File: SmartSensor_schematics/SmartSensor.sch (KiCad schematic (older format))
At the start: 47 parts, among them IC1 DS1337+, J1 Conn_01x07_Female, J3 Conn_02x04_Odd_Even, J4 FTDI cable connector, J6 Barrel_Jack, J8 6 PIN ISP, Q1 MMBF170, Q2 MMBF170, Q3 MMBF170, Q4 MMBF170, Q5 MMBF170, SW1 SW_Push, U1 AZ1117-3.3, U2 MCP9808_MSOP, U3 DMG2301l, U4 ATmega328-PU, U5 XBee_SMT, U6 MCP1640BCH, X1 XTAL

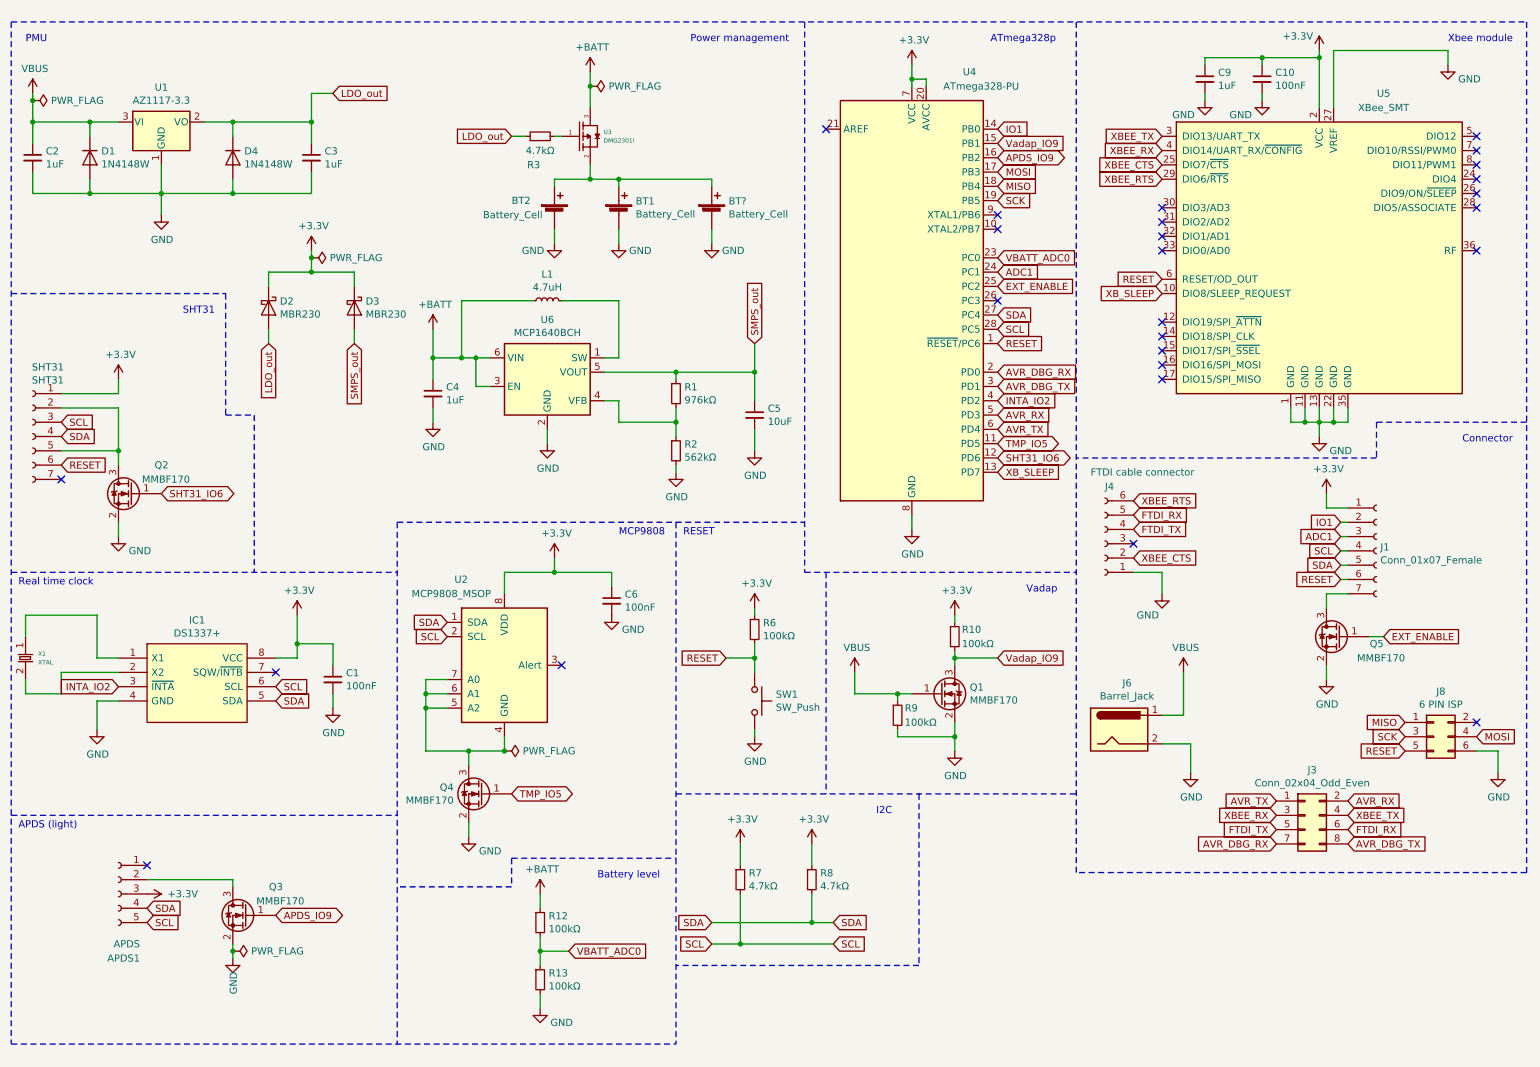
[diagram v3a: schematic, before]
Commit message: schematics: implement smart sensor v4
Implement version 4 in hardware.

Signed-off-by: Michel Megens <michel@michelmegens.net>
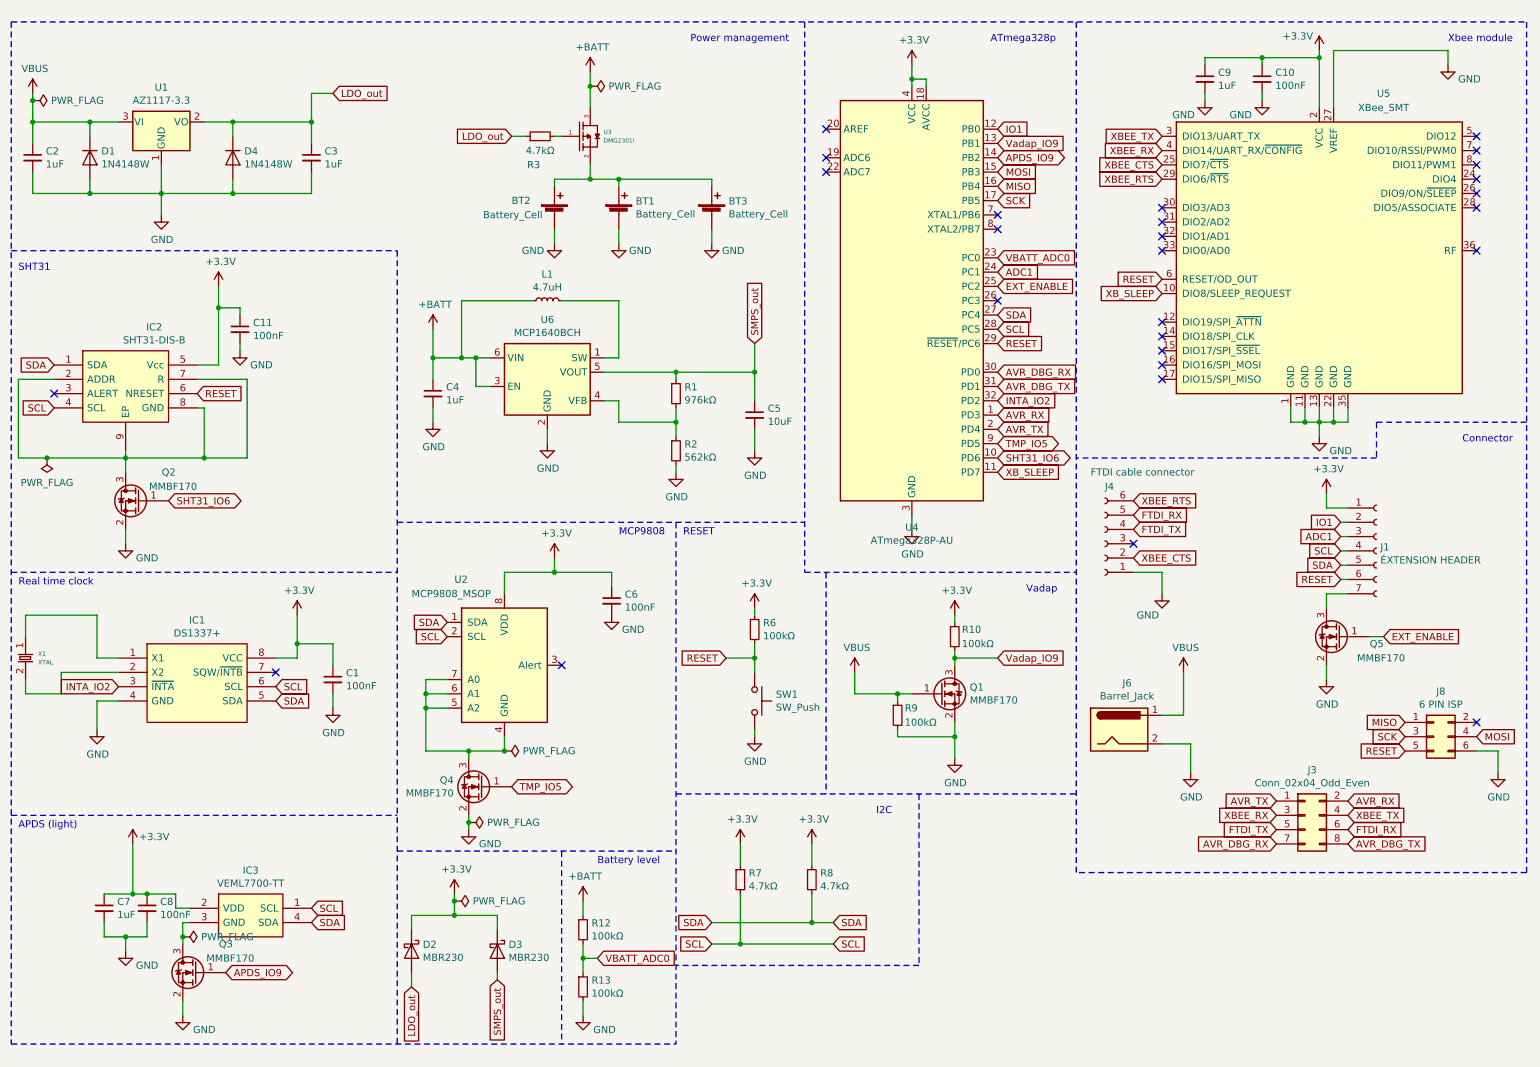
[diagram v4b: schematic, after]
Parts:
- removed APDS1: APDS, Connector_PinHeader_2.54mm:PinHeader_1x05_P2.54mm_Vertical, symbol Connector:Conn_01x05_Female
- removed SHT31: SHT31, Connector_PinHeader_2.54mm:PinHeader_1x07_P2.54mm_Vertical, symbol Connector:Conn_01x07_Female
- removed U4: ATmega328-PU, Package_DIP:DIP-28_W7.62mm, symbol MCU_Microchip_ATmega:ATmega328-PU
- added C11, C8: 100nF, Capacitor_SMD:C_1206_3216Metric_Pad1.42x1.75mm_HandSolder, symbol Device:C_Small
- added C7: 1uF, Capacitor_SMD:C_1206_3216Metric_Pad1.42x1.75mm_HandSolder, symbol Device:C_Small
- added IC2: SHT31-DIS-B, SHT31-DIS-B:SON50P250X250X90-9N-D, symbol SHT31-DIS-B:SHT31-DIS-B
- added IC3: VEML7700-TT, VEML7700:VEML7700, symbol VEML7700-TT:VEML7700-TT
- added U4: ATmega328P-AU, Package_QFP:TQFP-32_7x7mm_P0.8mm, symbol MCU_Microchip_ATmega:ATmega328P-AU
- J1: value Conn_01x07_Female -> ÉXTENSION HEADER
- gave numbers to parts that had none: 1
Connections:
- net +3V3: now also C11.1, C7.1, C8.1, IC2.5 (Vcc), IC3.2 (VDD), U4.18 (AVCC), U4.4 (VCC), U4.6 (VCC)
- net ADC1: now also U4.24 (PC1)
- net APDS_IO9: now also U4.14 (PB2)
- net AVR_DBG_RX: now also U4.30 (PD0)
- net AVR_DBG_TX: now also U4.31 (PD1)
- net AVR_RX: now also U4.1 (PD3)
- net AVR_TX: now also U4.2 (PD4)
- net EXT_ENABLE: now also U4.25 (PC2)
- net GND: now also C11.2, C7.2, C8.2, U4.21 (GND), U4.3 (GND), U4.5 (GND)
- net INTA_IO2: now also U4.32 (PD2)
- net IO1: now also U4.12 (PB0)
- net MISO: now also U4.16 (PB4)
- net MOSI: now also U4.15 (PB3)
- net RESET: now also IC2.6 (NRESET), U4.29 (~RESET~/PC6)
- net SCK: now also U4.17 (PB5)
- net SCL: now also IC2.4 (SCL), IC3.1 (SCL), U4.28 (PC5)
- net SDA: now also IC2.1 (SDA), IC3.4 (SDA), U4.27 (PC4)
- net SHT31_IO6: now also U4.10 (PD6)
- net TMP_IO5: now also U4.9 (PD5)
- net VBATT_ADC0: now also U4.23 (PC0)
- net Vadap_IO9: now also U4.13 (PB1)
- net XB_SLEEP: now also U4.11 (PD7)
- net at Q2.3 (D): now also IC2.2 (ADDR), IC2.7 (R), IC2.8 (GND), IC2.9 (EP)
- net at Q3.3 (D): now also IC3.3 (GND)
- no-connect marks 26 -> 27
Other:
- note removed: "PMU"
- moved on the sheet: D2, D3, Q4, R12, R13

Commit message: hardware: update hardware
Update the smart sensor hardware.

Signed-off-by: Michel Megens <michel@michelmegens.net>
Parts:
- removed U4: ATmega328P-AU, Package_QFP:TQFP-32_7x7mm_P0.8mm, symbol MCU_Microchip_ATmega:ATmega328P-AU
- added U7: ATmega1284P-AU, Package_QFP:TQFP-44_10x10mm_P0.8mm, symbol MCU_Microchip_ATmega:ATmega1284P-AU
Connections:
- net +3V3: now also U7.17 (VCC), U7.27 (AVCC), U7.38 (VCC), U7.5 (VCC)
- net ADC1: now also U7.36 (PA1)
- net APDS_IO9: now also U7.42 (PB2)
- net AVR_DBG_RX: now also U7.9 (PD0)
- net AVR_DBG_TX: now also U7.10 (PD1)
- net AVR_RX: now also U7.11 (PD2)
- net AVR_TX: now also U7.12 (PD3)
- net EXT_ENABLE: now also U7.21 (PC2)
- net GND: now also U7.18 (GND), U7.28 (GND), U7.39 (GND), U7.6 (GND)
- net INTA_IO2: now also U7.16 (PD7)
- net IO1: now also U7.40 (PB0)
- net MISO: now also U7.2 (PB6)
- net MOSI: now also U7.1 (PB5)
- net RESET: now also U7.4 (~RESET)
- net SCK: now also U7.3 (PB7)
- net SCL: now also U7.19 (PC0)
- net SDA: now also U7.20 (PC1)
- net SHT31_IO6: now also U7.14 (PD5)
- net TMP_IO5: now also U7.13 (PD4)
- net VBATT_ADC0: now also U7.37 (PA0)
- net Vadap_IO9: now also U7.41 (PB1)
- net XB_SLEEP: now also U7.15 (PD6)
- no-connect marks 27 -> 37
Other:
- moved on the sheet: Q1, R10, R6, R7, R8, R9, SW1
